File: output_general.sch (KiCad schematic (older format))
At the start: 13 parts, among them Q4 DMN65D8L, Q5 DMN65D8L, Q6 DMN65D8L, Q7 DMN65D8L, Q8 DMN65D8L, Q9 DMN65D8L

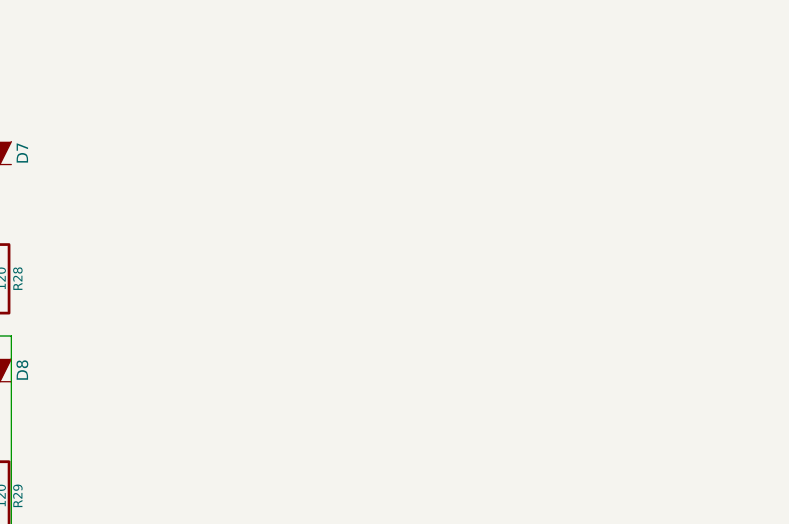
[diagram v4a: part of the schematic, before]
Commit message: finished routing board, added vibrator module
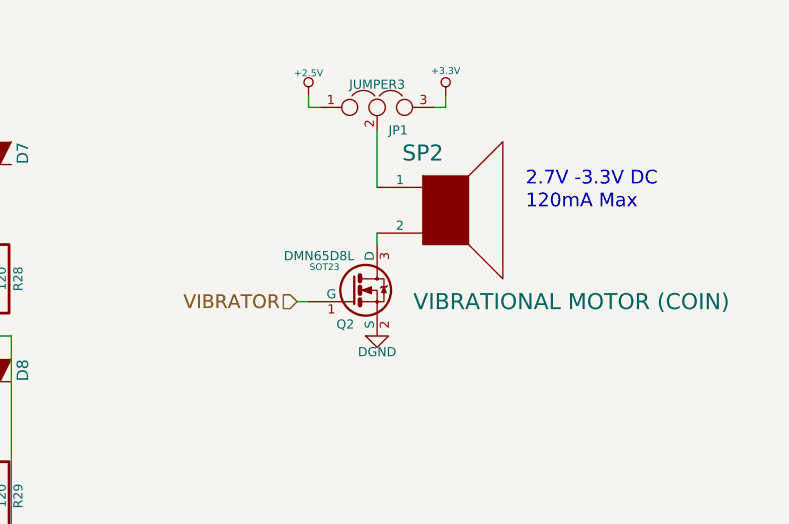
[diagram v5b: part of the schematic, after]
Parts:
- added JP1: JUMPER3, ~, symbol JUMPER3
- added Q2: DMN65D8L, SOT23, symbol DMN65D8L
- added SP2: VIBRATIONAL MOTOR (COIN), ~, symbol SPEAKER
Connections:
- net +3.3V: now also JP1.3
- net DGND: now also Q2.2 (S)
- new net: Q2.3 (D), SP2.2
- new net: JP1.2, SP2.1
- new net +2.5V: JP1.1
- new net VIBRATOR: Q2.1 (G)
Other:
- note added: "120mA Max"
- note added: "2.7V -3.3V DC"
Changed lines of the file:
@@
 $Descr A4 11693 8268
 encoding utf-8
-Sheet 8 16
+Sheet 16 16
 Title ""
-Date "16 feb 2014"
+Date "17 feb 2014"
 Rev ""
 Comp ""
@@
 $EndComp
 $Comp
-L DGND #PWR045
+L DGND #PWR0109
 U 1 1 528035E5
 P 1050 1250
-F 0 "#PWR045" H 1050 1250 40  0001 C CNN
+F 0 "#PWR0109" H 1050 1250 40  0001 C CNN
 F 1 "DGND" H 1050 1180 40  0000 C CNN
 F 2 "" H 1050 1250 60  0000 C CNN
@@
 $EndComp
 $Comp
-L DGND #PWR046
+L DGND #PWR0110
 U 1 1 528040AE
 P 3300 3750
-F 0 "#PWR046" H 3300 3750 40  0001 C CNN
+F 0 "#PWR0110" H 3300 3750 40  0001 C CNN
 F 1 "DGND" H 3300 3680 40  0000 C CNN
 F 2 "" H 3300 3750 60  0000 C CNN
@@
 $EndComp
 $Comp
-L DGND #PWR047
+L DGND #PWR0111
 U 1 1 528040B4
 P 3450 4250
-F 0 "#PWR047" H 3450 4250 40  0001 C CNN
+F 0 "#PWR0111" H 3450 4250 40  0001 C CNN
 F 1 "DGND" H 3450 4180 40  0000 C CNN
 F 2 "" H 3450 4250 60  0000 C CNN
@@
 $EndComp
 $Comp
-L DGND #PWR048
+L DGND #PWR0112
 U 1 1 528040BA
 P 3600 4750
-F 0 "#PWR048" H 3600 4750 40  0001 C CNN
+F 0 "#PWR0112" H 3600 4750 40  0001 C CNN
 F 1 "DGND" H 3600 4680 40  0000 C CNN
 F 2 "" H 3600 4750 60  0000 C CNN
@@
 $EndComp
 $Comp
-L +3.3V #PWR049
+L +3.3V #PWR0113
 U 1 1 52804204
 P 2600 650
-F 0 "#PWR049" H 2600 610 30  0001 C CNN
+F 0 "#PWR0113" H 2600 610 30  0001 C CNN
 F 1 "+3.3V" H 2600 760 30  0000 C CNN
 F 2 "" H 2600 650 60  0000 C CNN
@@
 	2600 650  2600 750
 $Comp
-L +3.3V #PWR050
+L +3.3V #PWR0114
 U 1 1 52804290
 P 2600 1600
-F 0 "#PWR050" H 2600 1560 30  0001 C CNN
+F 0 "#PWR0114" H 2600 1560 30  0001 C CNN
 F 1 "+3.3V" H 2600 1710 30  0000 C CNN
 F 2 "" H 2600 1600 60  0000 C CNN
@@
 $EndComp
 $Comp
-L +3.3V #PWR051
+L +3.3V #PWR0115
 U 1 1 52804296
 P 2600 2550
-F 0 "#PWR051" H 2600 2510 30  0001 C CNN
+F 0 "#PWR0115" H 2600 2510 30  0001 C CNN
 F 1 "+3.3V" H 2600 2660 30  0000 C CNN
 F 2 "" H 2600 2550 60  0000 C CNN
@@
 Wire Wire Line
 	2600 4600 3300 4600
+Text HLabel 4850 1750 0    60   Input ~ 0
+VIBRATOR
+$Comp
+L DMN65D8L Q2
+U 1 1 5301CDA5
+P 5100 1700
+F 0 "Q2" H 5100 1551 40  0000 R CNN
+F 1 "DMN65D8L" H 5100 1850 40  0000 R CNN
+F 2 "SOT23" H 4970 1802 29  0000 C CNN
+F 3 "~" H 5100 1700 60  0000 C CNN
+	1    5100 1700
+	1    0    0    -1
+$EndComp
+$Comp
+L JUMPER3 JP1
+U 1 1 5301CDAD
+P 5200 900
+F 0 "JP1" H 5250 800 40  0000 L CNN
+F 1 "JUMPER3" H 5200 1000 40  0000 C CNN
+F 2 "~" H 5200 900 60  0000 C CNN
+F 3 "~" H 5200 900 60  0000 C CNN
+	1    5200 900
+	1    0    0    -1
+$EndComp
+$Comp
+L SPEAKER SP2
+U 1 1 5301CDBA
+P 5500 1350
+F 0 "SP2" H 5400 1600 70  0000 C CNN
+F 1 "VIBRATIONAL MOTOR (COIN)" H 6050 950 70  0000 C CNN
+F 2 "~" H 5500 1350 60  0000 C CNN
+F 3 "~" H 5500 1350 60  0000 C CNN
+	1    5500 1350
+	1    0    0    -1
+$EndComp
+Wire Wire Line
+	4900 1750 4850 1750
+$Comp
+L DGND #PWR0116
+U 1 1 5301CE04
+P 5200 1900
+F 0 "#PWR0116" H 5200 1900 40  0001 C CNN
+F 1 "DGND" H 5200 1830 40  0000 C CNN
+F 2 "" H 5200 1900 60  0000 C CNN
+F 3 "" H 5200 1900 60  0000 C CNN
+	1    5200 1900
+	1    0    0    -1
+$EndComp
+Wire Wire Line
+	5200 1450 5200 1500
+Wire Wire Line
+	5200 1250 5200 1000
+$Comp
+L +3.3V #PWR0117
+U 1 1 5301CE9A
+P 5500 850
+F 0 "#PWR0117" H 5500 810 30  0001 C CNN
+F 1 "+3.3V" H 5500 960 30  0000 C CNN
+F 2 "" H 5500 850 60  0000 C CNN
+F 3 "" H 5500 850 60  0000 C CNN
+	1    5500 850
+	1    0    0    -1
+$EndComp
+Wire Wire Line
+	5450 900  5500 900
+Wire Wire Line
+	5500 900  5500 850
+Text Notes 5850 1350 0    60   ~ 0
+120mA Max
+Text Notes 5850 1250 0    60   ~ 0
+2.7V -3.3V DC
+$Comp
+L +2.5V #PWR0118
+U 1 1 53020E56
+P 4900 850
+F 0 "#PWR0118" H 4900 800 20  0001 C CNN
+F 1 "+2.5V" H 4900 950 30  0000 C CNN
+F 2 "" H 4900 850 60  0000 C CNN
+F 3 "" H 4900 850 60  0000 C CNN
+	1    4900 850
+	1    0    0    -1
+$EndComp
+Wire Wire Line
+	4900 850  4900 900
+Wire Wire Line
+	4900 900  4950 900
 $EndSCHEMATC
